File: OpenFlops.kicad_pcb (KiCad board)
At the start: 2 copper layers, 111.6 x 59.4 mm, 82 parts, among them J99 OSHW_LOGO, P1 FLOPPY_CONN, P2 POWER_INPUT, P3 USB_A_FEMALE, P4 PROG_PORT, P5 JUMPERS, P6 ENCODER_PORT, P7 DISPLAY_PORT, P8 USB_HEADER, P9 EXTERNAL_SPEAKER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

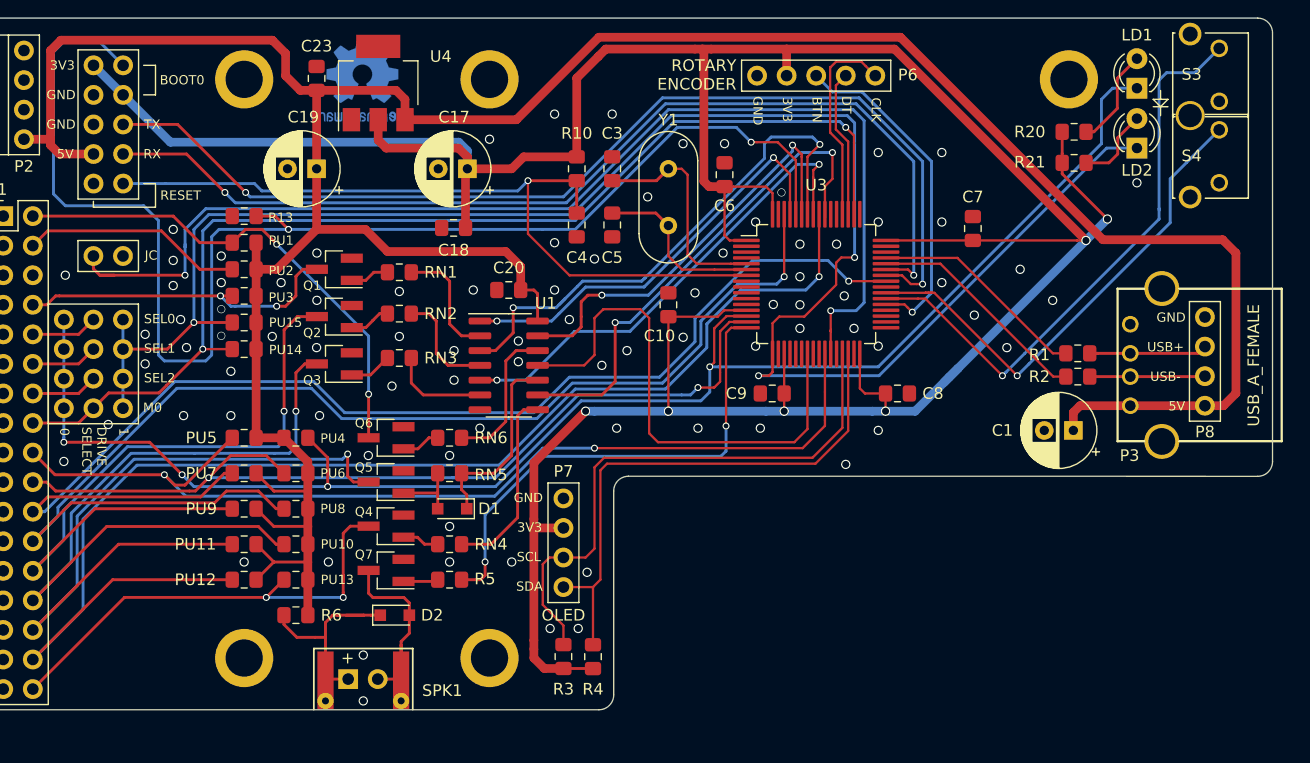
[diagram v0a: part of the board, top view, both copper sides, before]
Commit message: Add BOOT1 testpoint and lots of changes for auto P&P
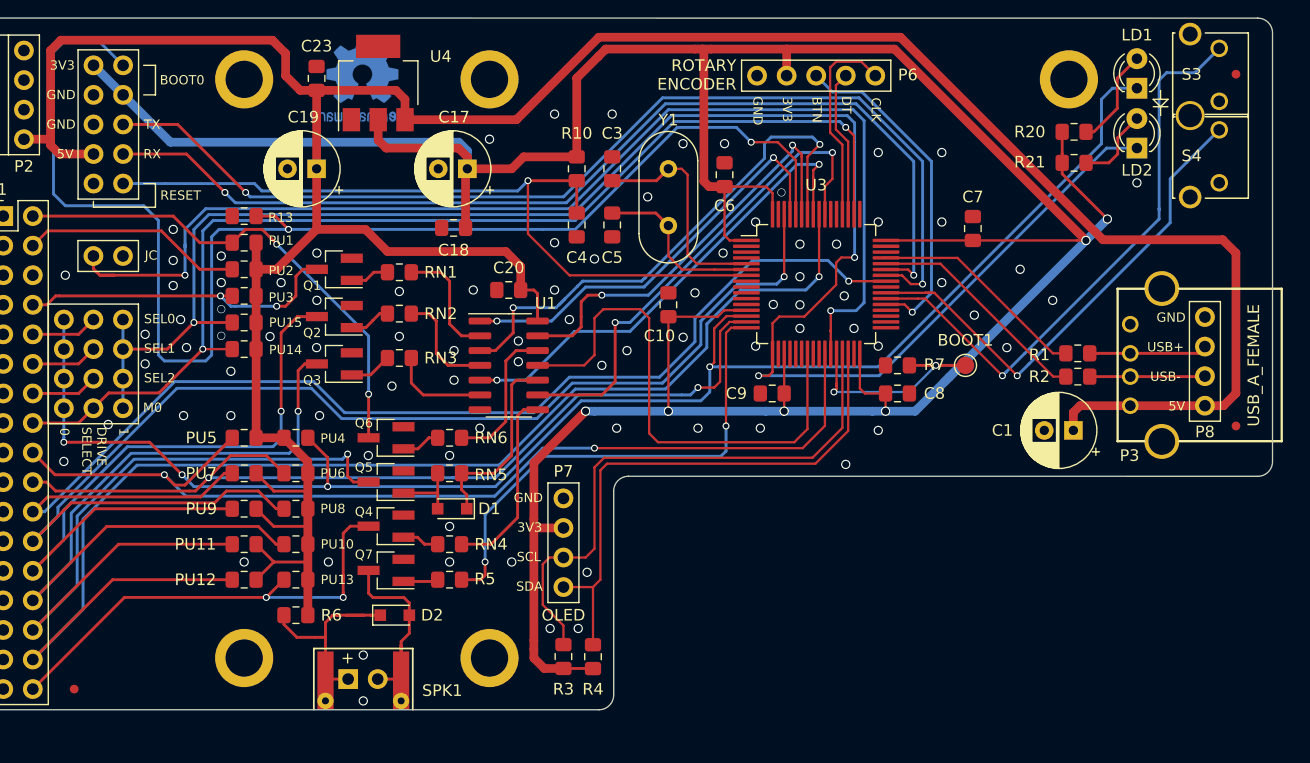
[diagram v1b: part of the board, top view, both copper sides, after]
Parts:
- added FID1: Fiducial, Fiducial:Fiducial_0.75mm_Mask1.5mm, F.Cu at (103.9, 113.0)
- added FID2: Fiducial, Fiducial:Fiducial_0.75mm_Mask1.5mm, F.Cu at (203.7, 60.2)
- added FID3: Fiducial, Fiducial:Fiducial_0.75mm_Mask1.5mm, F.Cu at (203.7, 90.4)
- added R7: 4k7, Resistor_SMD:R_0805_2012Metric_Pad1.15x1.40mm_HandSolder, F.Cu at (174.6, 85.2)
- added TP1: BOOT1, TestPoint:TestPoint_Pad_D1.5mm, F.Cu at (180.5, 85.2)
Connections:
- U3 pad 28: GND -> /boot1
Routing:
- net /boot1: track 0.00 -> 17.9 mm, vias 0 -> 2
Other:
- board text added: "BOOT1"
- board text added: "V1B"
- board text removed: "V1"

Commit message: Some refinements
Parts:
- TP1: footprint TestPoint:TestPoint_Pad_D1.5mm -> TestPoint:TestPoint_Pad_D1.0mm
- moved TP1 5.24 mm to (175.6, 83.2)
- moved R1 0.44 mm to (190.6, 84.2)
- moved R2 0.44 mm to (190.6, 86.2)
- moved R7 0.13 mm to (174.6, 85.3)
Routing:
- net /boot1: track 17.9 -> 15.4 mm
- net Net-(S3-Pad2): track 50.5 -> 52.2 mm
- net GND: vias 86 -> 91

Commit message: Final touches for V1final
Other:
- board text added: "V1"
- board text removed: "V1B"
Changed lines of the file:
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@@
-(kicad_pcb (version 20171130) (host pcbnew 5.1.2)
+(kicad_pcb (version 20171130) (host pcbnew 5.1.5)
   (general
     (thickness 1.6)
@@
   (title_block
     (title OpenFlops)
-    (date 2019-10-09)
-    (rev 1git)
+    (date 2020-01-01)
+    (rev 1)
     (company SukkoPera)
     (comment 1 "Licensed under CERN OHL v.1.2")
@@
     (46 B.CrtYd user hide)
     (47 F.CrtYd user hide)
-    (49 F.Fab user hide)
+    (49 F.Fab user)
   )
   (setup
-    (last_trace_width 0.2)
+    (last_trace_width 0.25)
     (user_trace_width 0.2)
     (user_trace_width 0.25)
@@
     (pad 1 smd rect (at 0 -1.75) (size 1.4 5) (layers F.Cu F.Mask)
       (net 61 /spk+))
-    (pad 2 thru_hole circle (at 6.5 0) (size 1.4 1.4) (drill 0.6) (layers *.Cu *.Mask)
+    (pad 2 thru_hole circle (at 6.5 0) (size 1.4 1.4) (drill 0.8) (layers *.Cu *.Mask)
       (net 60 /spk-))
-    (pad 1 thru_hole circle (at 0 0) (size 1.4 1.4) (drill 0.6) (layers *.Cu *.Mask)
+    (pad 1 thru_hole circle (at 0 0) (size 1.4 1.4) (drill 0.8) (layers *.Cu *.Mask)
       (net 61 /spk+))
-    (model ${KISYS3DMOD}/Buzzer_Beeper.3dshapes/Buzzer_12x9.5RM7.6.step
-      (offset (xyz 0 -1 0.5))
+    (model ${KISYS3DMOD}/Buzzer_Beeper.3dshapes/Buzzer_12x9.5RM7.6.wrl
+      (offset (xyz 0 -0.8 0.5))
       (scale (xyz 0.85 0.85 1))
       (rotate (xyz -90 0 0))
@@
       (effects (font (size 1 1) (thickness 0.15)))
     )
-    (fp_text value EXTERNAL_SPEAKER (at 0 4.87 90) (layer F.Fab)
+    (fp_text value EXTERNAL_SPEAKER (at 0 4.87 90) (layer F.Fab) hide
       (effects (font (size 1 1) (thickness 0.15)))
     )
@@
     (effects (font (size 0.8 0.8) (thickness 0.12)))
   )
-  (gr_text V1B (at 148.082 113.538) (layer B.SilkS)
+  (gr_text V1 (at 148.082 113.538) (layer B.SilkS)
     (effects (font (size 1 1) (thickness 0.15)) (justify mirror))
   )

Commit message: Fixes for BOM
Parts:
- D1, D2: value 1N5819 (?) -> 1N4148
- P5: value JUMPERS -> JUMPER_JC
- Q1, Q2, Q3, Q4, Q5, Q6: value MOS_N_GSD -> BSS138

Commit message: Add files via upload
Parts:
- added P10: SD CARD, OpenFlops:PinHeader_1x05_P2.54mm_Vertical, F.Cu at (183.4, 92.0)
- added P11: SD PWR, OpenFlops:PinHeader_1x02_P2.54mm_Vertical, F.Cu at (170.7, 92.0)
- added P12: SD DISABLE, OpenFlops:PinHeader_1x02_P2.54mm_Vertical, F.Cu at (108.0, 107.5)
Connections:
- net /~dskchg renamed /~{dskchg}
- net /~dskchg_3v3 renamed /~{dskchg_3v3}
- net /~index renamed /~{index}
- net /~index_3v3 renamed /~{index_3v3}
- net /~inuse renamed /~{inuse}
- net /~mtron renamed /~{mtron}
- net /~rdata renamed /~{rdata}
- net /~rdata_3v3 renamed /~{rdata_3v3}
- net /~rdy renamed /~{rdy}
- net /~sel0 renamed /~{sel0}
- net /~sel1 renamed /~{sel1}
- net /~sel2 renamed /~{sel2}
- net /~selx renamed /~{selx}
- net /~sely renamed /~{sely}
- net /~side renamed /~{side}
- net /~trk0_3v3 renamed /~{trk0_3v3}
- net /~wprot renamed /~{wprot}
- net /~wprot_3v3 renamed /~{wprot_3v3}
- C3 pad 1: Net-(C3-Pad1) -> (no net)
- C5 pad 1: Net-(C5-Pad1) -> (no net)
- P1 pad 18: /dir -> (no net)
- P1 pad 20: /~step -> (no net)
- P1 pad 22: /~wdata -> (no net)
- P1 pad 24: /~wgate -> (no net)
- P1 pad 26: /~trk0 -> (no net)
- P1 pad 6: (no net) -> /~{sel3}
- P2 pad 4: (no net) -> unconnected-(P2-Pad4)
- PU6 pad 2: /~step -> /dir
- PU7 pad 2: /~wdata -> /dir
- PU8 pad 2: /~wgate -> /dir
- PU9 pad 2: /~trk0 -> /dir
- Q2 pad 3: /~trk0 -> /dir
- U1 pad 9: /~rdy_3v3 -> unconnected-(U1-Pad9)
- U3 pad 10: (no net) -> unconnected-(U3-Pad10)
- U3 pad 11: (no net) -> unconnected-(U3-Pad11)
- U3 pad 15: /~step -> /dir
- U3 pad 20: (no net) -> unconnected-(U3-Pad20)
- U3 pad 21: (no net) -> unconnected-(U3-Pad21)
- U3 pad 22: (no net) -> unconnected-(U3-Pad22)
- U3 pad 24: (no net) -> unconnected-(U3-Pad24)
- U3 pad 25: (no net) -> unconnected-(U3-Pad25)
- U3 pad 33: (no net) -> /spi_cs
- U3 pad 34: (no net) -> /spi_clk
- U3 pad 35: (no net) -> /spi_do
- U3 pad 36: (no net) -> /spi_di
- U3 pad 40: (no net) -> /spi_cd
- U3 pad 41: /~wdata -> /dir
- U3 pad 46: (no net) -> unconnected-(U3-Pad46)
- U3 pad 49: (no net) -> /swclk
- U3 pad 53: GND -> Net-(P12-Pad1)
- U3 pad 54: (no net) -> unconnected-(U3-Pad54)
- U3 pad 55: /~rdy_3v3 -> /~{rdy_3v3}
- U3 pad 62: /~wgate -> /dir
- U3 pad 8: (no net) -> unconnected-(U3-Pad8)
- U3 pad 9: (no net) -> unconnected-(U3-Pad9)
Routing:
- net /dir: track 86.6 -> 434.7 mm, vias 2 -> 7
- net /~wgate: track 106.8 -> 0.00 mm, vias 1 -> 0
- net /~wdata: track 104.9 -> 0.00 mm, vias 1 -> 0
- net Net-(P12-Pad1): track 0.00 -> 93.6 mm, vias 0 -> 3
- net /~step: track 78.5 -> 0.00 mm, vias 2 -> 0
- net /~trk0: track 59.3 -> 0.00 mm, vias 1 -> 0
- net /~rdy_3v3: track 42.8 -> 0.00 mm, vias 2 -> 0
- net /~{rdy_3v3}: track 0.00 -> 42.8 mm, vias 0 -> 2
- net /spi_cd: track 0.00 -> 23.4 mm
- net /spi_clk: track 0.00 -> 21.1 mm, vias 0 -> 1
- net /spi_do: track 0.00 -> 20.8 mm, vias 0 -> 1
- net /spi_di: track 0.00 -> 20.6 mm, vias 0 -> 1
- net /spi_cs: track 0.00 -> 18.1 mm, vias 0 -> 1
- net +3V3: track 288.7 -> 296.7 mm
- net /~{rdy}: track 40.7 -> 44.1 mm
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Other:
- net class Default removed
- net class Power removed
- net class uC removed
- board text added: "CD"
- board text added: "CS"
- board text added: "DI"
- board text added: "DO"
- board text added: "Licensed under CERN OHL v.1.3"
- board text added: "SD CARD MODULE"
- board text added: "V1.3"
- board text removed: "Licensed under CERN OHL v.1.2"
- board text removed: "V1"

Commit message: Refine design
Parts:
- removed FID1, FID2, FID3: Fiducial, Fiducial:Fiducial_0.75mm_Mask1.5mm
- P12: value SD DISABLE -> SD_DISABLE
- moved P12 0.08 mm to (108.1, 107.5)
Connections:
- C3 pad 1: (no net) -> Net-(C3-Pad1)
- C5 pad 1: (no net) -> Net-(C5-Pad1)
- P1 pad 18: (no net) -> /dir
- P1 pad 20: (no net) -> /~{step}
- P1 pad 22: (no net) -> /~{wdata}
- P1 pad 24: (no net) -> /~{wgate}
- P1 pad 26: (no net) -> /~{trk0}
- PU6 pad 2: /dir -> /~{step}
- PU7 pad 2: /dir -> /~{wdata}
- PU8 pad 2: /dir -> /~{wgate}
- PU9 pad 2: /dir -> /~{trk0}
- Q2 pad 3: /dir -> /~{trk0}
- U1 pad 9: unconnected-(U1-Pad9) -> /~{rdy_3v3}
- U3 pad 15: /dir -> /~{step}
- U3 pad 41: /dir -> /~{wdata}
- U3 pad 62: /dir -> /~{wgate}
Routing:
- net /dir: track 434.7 -> 86.4 mm, vias 7 -> 2
- net /~{wgate}: track 0.00 -> 106.4 mm, vias 0 -> 1
- net /~{wdata}: track 0.00 -> 104.9 mm, vias 0 -> 1
- net /~{step}: track 0.00 -> 78.1 mm, vias 0 -> 2
- net /~{trk0}: track 0.00 -> 58.4 mm, vias 0 -> 1
- net Net-(U3-Pad53): track 93.6 -> 91.0 mm
- net /~{rdata}: track 60.9 -> 59.1 mm
- net /spk+: track 18.6 -> 16.8 mm
- net /jc: track 99.9 -> 98.4 mm
- net /~{side}: track 114.3 -> 113.0 mm
- net /jb: track 41.9 -> 40.9 mm
- net /~{wprot}: track 64.0 -> 63.1 mm
- net /~{trk0_3v3}: track 46.7 -> 45.8 mm
- net Net-(S4-Pad2): track 43.8 -> 43.2 mm
- net /~{rdy}: track 44.1 -> 43.4 mm
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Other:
- board text added: "V1.4"
- board text removed: "V1.3"
